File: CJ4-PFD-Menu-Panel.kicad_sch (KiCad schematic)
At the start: 34 parts, among them J3 BARO encoder, J4 MENU ADV and DATA encoder, J5 TILT and RANGE encoder, J6 Conn_01x02, J7 Conn_01x02, SW10 SW_PUSH_LED, SW11 SW_PUSH_LED, SW12 SW_PUSH_LED, SW13 SW_PUSH_LED, SW3 SW_PUSH_LED, SW4 SW_PUSH_LED, SW5 SW_PUSH_LED, SW6 SW_PUSH_LED, SW7 SW_PUSH_LED, SW8 SW_PUSH_LED, SW9 SW_PUSH_LED, U2 DM13A

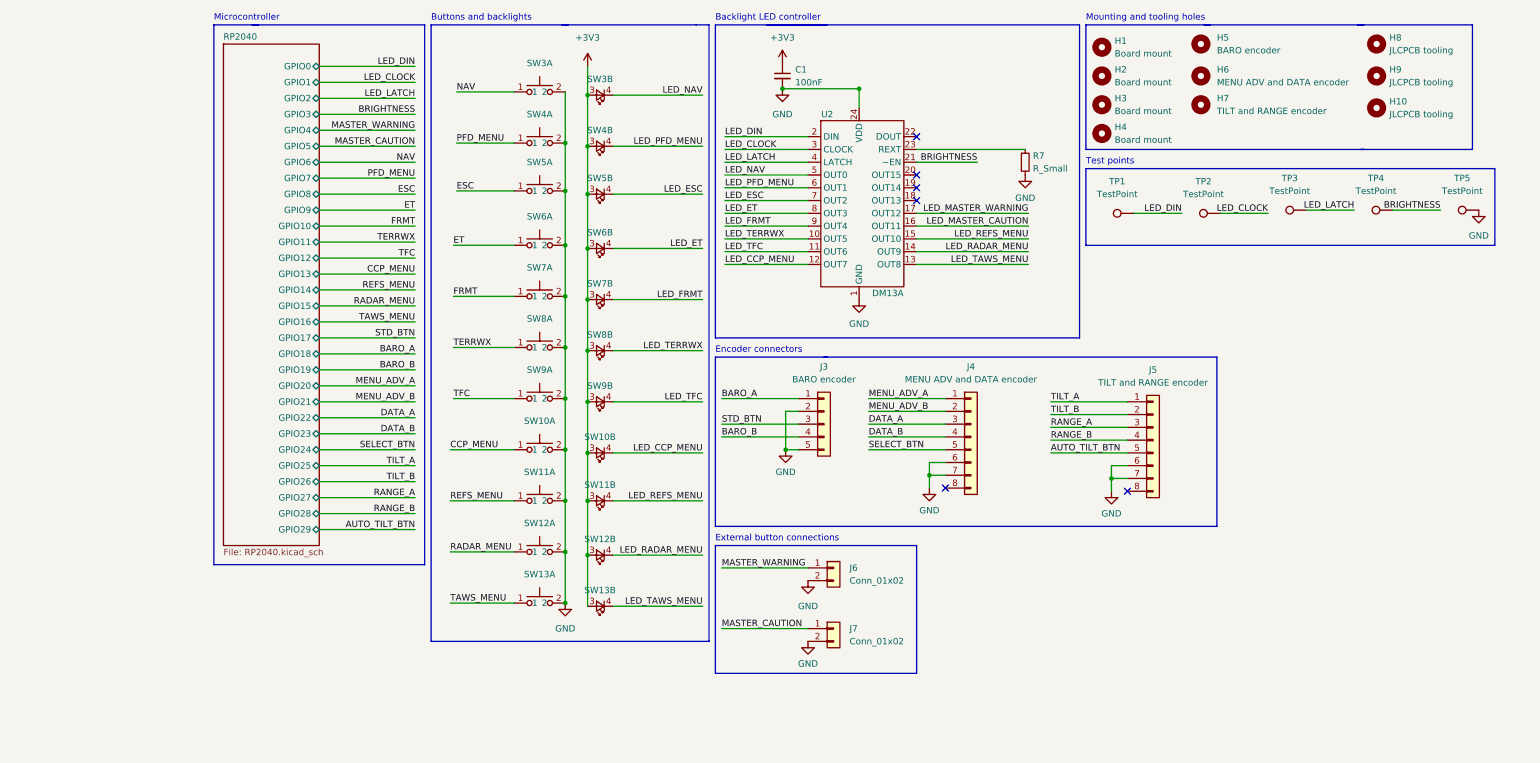
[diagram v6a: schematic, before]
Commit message: Redo RP2040 layout
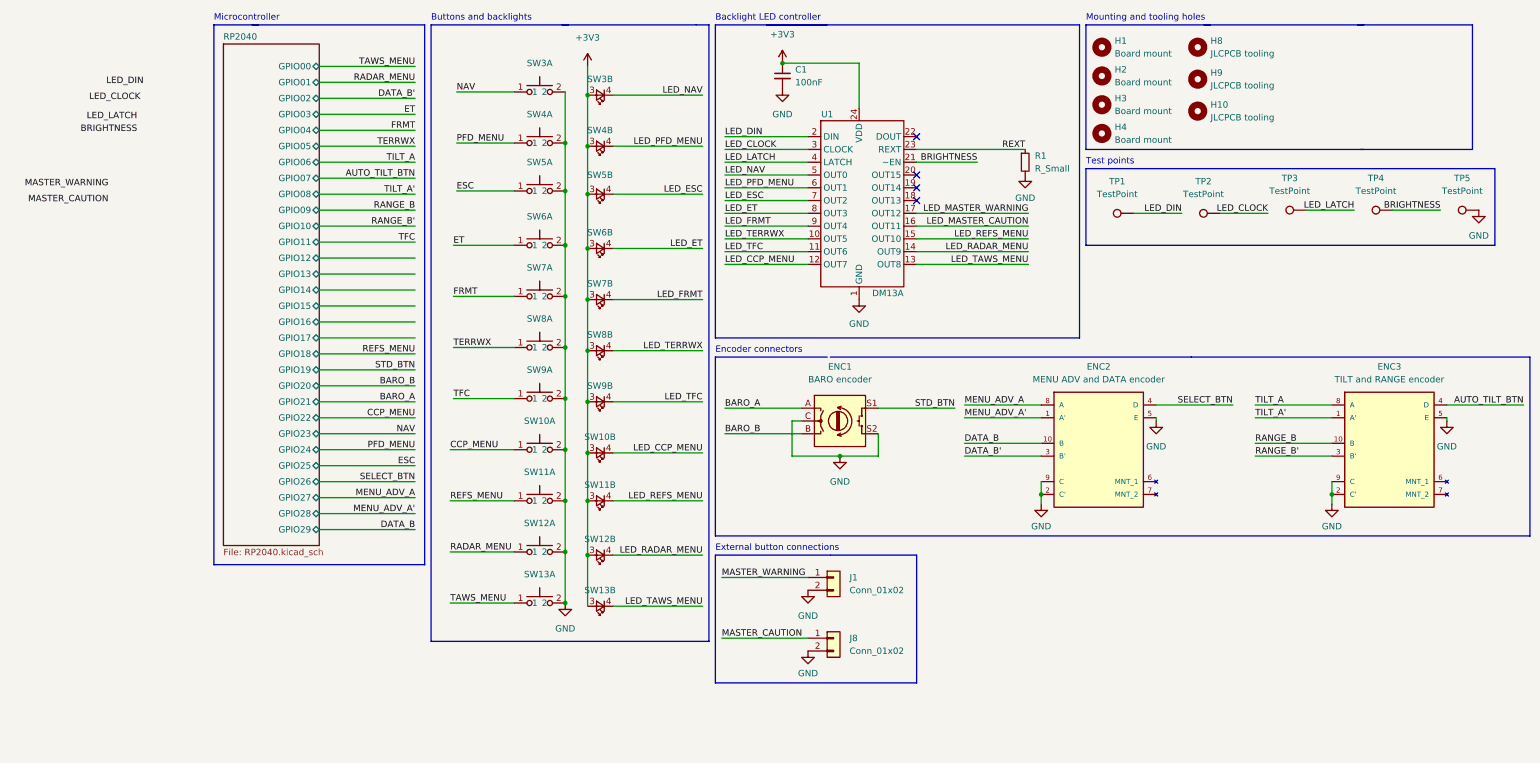
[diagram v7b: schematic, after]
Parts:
- removed H5: BARO encoder, Custom_Footprints:EN11-HSM1BF20_PM, symbol Mechanical:MountingHole
- removed H6: MENU ADV and DATA encoder, Custom_Footprints:EC11E-BB24C03_PM, symbol Mechanical:MountingHole
- removed H7: TILT and RANGE encoder, Custom_Footprints:EC11E-BB24C03_PM, symbol Mechanical:MountingHole
- removed J3: BARO encoder, Connector_JST:JST_XH_B5B-XH-A_1x05_P2.50mm_Vertical, symbol Connector_Generic:Conn_01x05
- removed J4: MENU ADV and DATA encoder, Connector_JST:JST_XH_B8B-XH-A_1x08_P2.50mm_Vertical, symbol Connector_Generic:Conn_01x08
- removed J5: TILT and RANGE encoder, Connector_JST:JST_XH_B8B-XH-A_1x08_P2.50mm_Vertical, symbol Connector_Generic:Conn_01x08
- added ENC1: BARO encoder, Custom_Footprints:EN11-HSM1BF20_THT, symbol Device:RotaryEncoder_Switch
- added ENC2: MENU ADV and DATA encoder, Custom_Footprints:ALPS-EC11EBB24C03-0, symbol Custom_Symbols:EC11EBB24C03
- added ENC3: TILT and RANGE encoder, Custom_Footprints:ALPS-EC11EBB24C03-0, symbol Custom_Symbols:EC11EBB24C03
- renumbered J6 to J1, J7 to J8, R7 to R1, U2 to U1
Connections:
- net +3V3: now also U1.24 (VDD)
- net AUTO_TILT_BTN: now also ENC3.4 (D)
- net BARO_A: now also ENC1.A
- net BARO_B: now also ENC1.B
- net DATA_B: now also ENC2.10 (B)
- net GND: now also ENC1.C, ENC1.S2, ENC2.2 (C'), ENC2.5 (E), ENC2.9 (C), ENC3.2 (C'), ENC3.5 (E), ENC3.9 (C); no longer U1.24 (VDD)
- net MENU_ADV_A: now also ENC2.8 (A)
- net RANGE_B: now also ENC3.10 (B)
- net SELECT_BTN: now also ENC2.4 (D)
- net STD_BTN: now also ENC1.S1
- net TILT_A: now also ENC3.8 (A)
- net REXT: now reaches R1.1, U1.23 (REXT)
- new net DATA_B': ENC2.3 (B')
- new net MENU_ADV_A': ENC2.1 (A')
- new net RANGE_B': ENC3.3 (B')
- new net TILT_A': ENC3.1 (A')
- no-connect marks 6 -> 4
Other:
- sheet RP2040 ports: added GPIO00, GPIO01, GPIO02, GPIO03, GPIO04, GPIO05, GPIO06, GPIO07, GPIO08, GPIO09; removed GPIO0, GPIO1, GPIO2, GPIO3, GPIO4, GPIO5, GPIO6, GPIO7, GPIO8, GPIO9
- moved on the sheet: H10, H8, H9, J1, J8

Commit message: Fully routed!
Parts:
- J1, J8: footprint Connector_JST:JST_XH_B2B-XH-A_1x02_P2.50mm_Vertical -> Connector_JST:JST_XH_B3B-XH-A_1x03_P2.50mm_Vertical; symbol Connector_Generic:Conn_01x02 -> Connector_Generic:Conn_01x03
- SW10, SW11, SW12, SW13, SW3, SW4, SW5, SW6, SW7, SW8, SW9: footprint Custom_Footprints:SW_PUSH_LED_SMD -> Custom_Footprints:SW_PUSH_LED_THT
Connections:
- net LED_MASTER_CAUTION is gone; now on net LED_FRMT: U1.16 (OUT11)
- net LED_MASTER_WARNING is gone; now on net LED_TERRWX: U1.17 (OUT12)
- net GND: now also J1.3 (Pin_3), J8.3 (Pin_3); no longer J1.2 (Pin_2), J8.2 (Pin_2)
- net LED_CCP_MENU: now also U1.20 (OUT15); no longer U1.12 (OUT7)
- net LED_ESC: now also U1.14 (OUT9); no longer U1.7 (OUT2)
- net LED_ET: now also U1.15 (OUT10); no longer U1.8 (OUT3)
- net LED_FRMT: no longer U1.9 (OUT4)
- net LED_NAV: now also U1.12 (OUT7); no longer U1.5 (OUT0)
- net LED_PFD_MENU: now also U1.13 (OUT8); no longer U1.6 (OUT1)
- net LED_RADAR_MENU: now also U1.18 (OUT13); no longer U1.14 (OUT9)
- net LED_REFS_MENU: now also U1.19 (OUT14); no longer U1.15 (OUT10)
- net LED_TAWS_MENU: now also U1.5 (OUT0); no longer U1.13 (OUT8)
- net LED_TERRWX: no longer U1.10 (OUT5)
- net LED_TFC: now also U1.6 (OUT1); no longer U1.11 (OUT6)
- net MASTER_CAUTION: now also J8.2 (Pin_2); no longer J8.1 (Pin_1)
- net MASTER_WARNING: now also J1.2 (Pin_2); no longer J1.1 (Pin_1)
- new net LED_CAUTION: J1.1 (Pin_1), U1.11 (OUT6)
- new net LED_WARNING: J8.1 (Pin_1), U1.10 (OUT5)
- no-connect marks 4 -> 1
